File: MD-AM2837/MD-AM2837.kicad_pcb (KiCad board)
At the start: 2 copper layers, 47 x 36 mm, 15 parts, among them J1 XT60_Male_Horizontal, J2 XT60_Female_Horizontal, J3 Conn_01x03_Pin_signal

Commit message: v0.1
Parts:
- added D1: 1N4007, Diode_THT:D_DO-41_SOD81_P10.16mm_Horizontal, F.Cu at (112.5, 87.7)
- added D2: 1N4007, Diode_THT:D_DO-41_SOD81_P10.16mm_Horizontal, F.Cu at (116.0, 87.6)
- added LED4: PWR, LED_SMD:LED_0603_1608Metric_Pad1.05x0.95mm_HandSolder, F.Cu at (90.0, 87.0)
- added Q1: BSS138, Package_TO_SOT_SMD:SOT-23, F.Cu at (106.6, 74.5)
- added Q2: BSS138, Package_TO_SOT_SMD:SOT-23, F.Cu at (106.4, 79.0)
- added R4: R10k, Resistor_SMD:R_0603_1608Metric_Pad0.98x0.95mm_HandSolder, F.Cu at (93.0, 86.1)
- C1: footprint Capacitor_SMD:C_Elec_10x10.2 -> Capacitor_THT:C_Radial_D8.0mm_H11.5mm_P3.50mm
- moved C1 7.40 mm to (125.0, 80.5)
- moved G*** 2.16 mm to (111.0, 82.5)
- moved J2 1.65 mm to (96.4, 91.0)
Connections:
- net Net-(J2-GND) renamed OUT_B
- net Net-(J2-VOUT) renamed OUT_A
- J3 pad 1: Net-(J3-Pin_1) -> IN_A
- J3 pad 2: Net-(J3-Pin_2) -> IN_B
- MD1 pad 1: Net-(J3-Pin_1) -> IN_A
- MD1 pad 2: Net-(J3-Pin_2) -> IN_B
- R1 pad 2: Net-(J3-Pin_1) -> Net-(Q1-D)
- R2 pad 2: Net-(J3-Pin_2) -> Net-(Q2-D)
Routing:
- net Net-(D1-K): track 0.00 -> 41.6 mm
- net Net-(Q1-D): track 0.00 -> 35.5 mm, vias 0 -> 2
- net Net-(J3-Pin_1): track 32.3 -> 0.00 mm
- net IN_A: track 0.00 -> 27.2 mm
- net OUT_B: track 30.2 -> 57.2 mm
- net Net-(J3-Pin_2): track 25.6 -> 0.00 mm
- net Net-(Q2-D): track 0.00 -> 24.0 mm, vias 0 -> 2
- net IN_B: track 0.00 -> 22.8 mm, vias 0 -> 2
- net OUT_A: track 30.5 -> 50.0 mm
- net Net-(LED4-K): track 0.00 -> 4.70 mm
- net VCC: track 97.4 -> 94.7 mm, vias 3 -> 2
- net GND: vias 21 -> 20
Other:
- board text added: "Female"
- board text added: "MD-AM2837 Sep. 11th 2025 Eita TSUGUTA"
- board text added: "Male"
- board text added: "ver. 0.1"
- board text removed: "MD using AM2837 Sep. 30th 2024 Eita TSUGUTA"
- board text removed: "XT60 Female"
- board text removed: "XT60 Male"

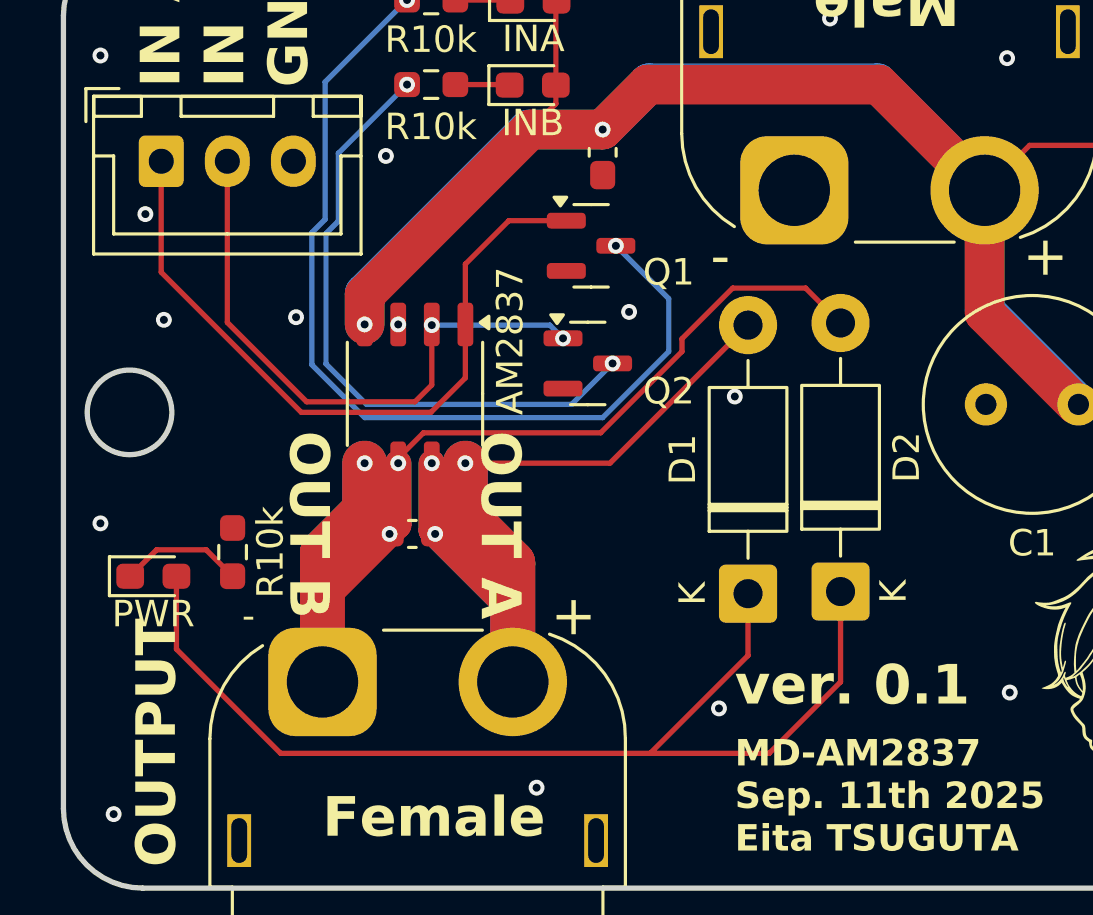
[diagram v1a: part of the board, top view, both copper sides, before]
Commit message: フォトカプラ追加中
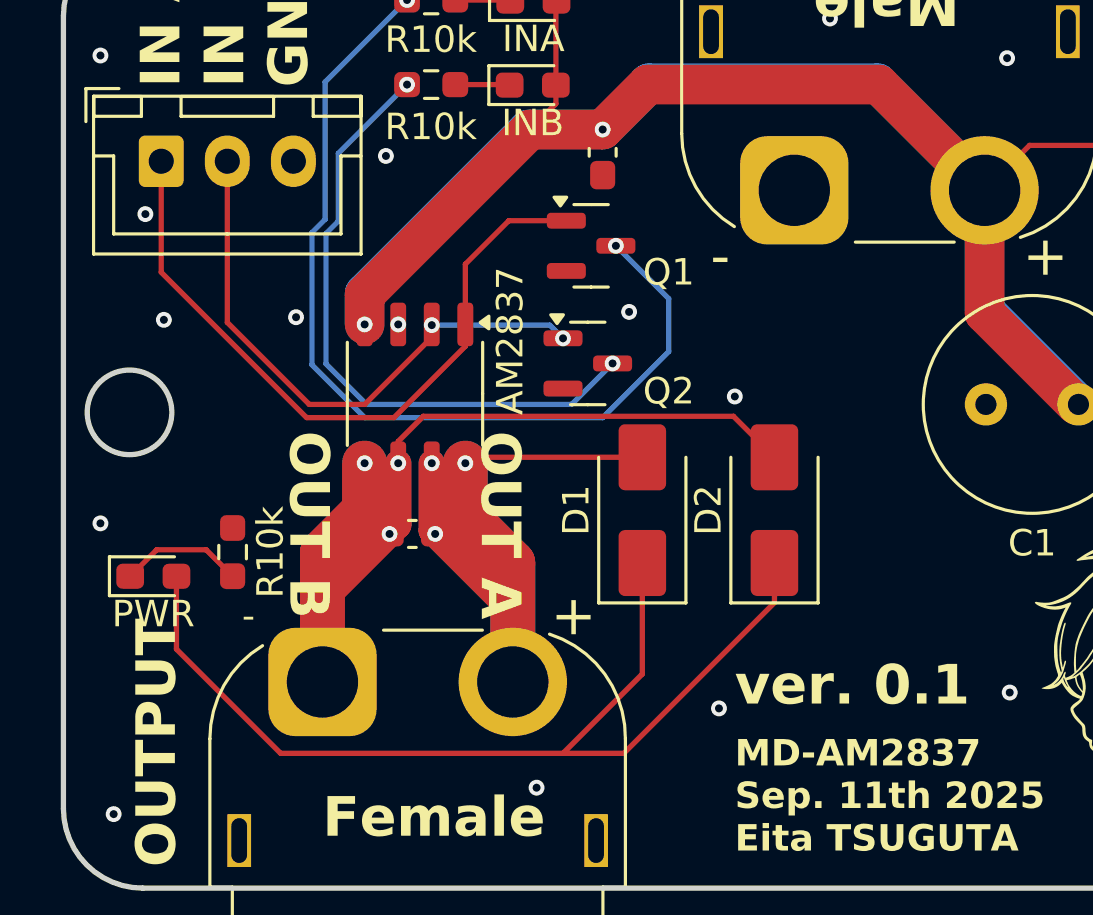
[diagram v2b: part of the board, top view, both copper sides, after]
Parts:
- D1, D2: value 1N4007 -> SS14; footprint Diode_THT:D_DO-41_SOD81_P10.16mm_Horizontal -> Diode_SMD:D_SMA
- moved D1 5.10 mm to (108.5, 84.5)
- moved D2 3.97 mm to (113.5, 84.5)
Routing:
- net OUT_A: track 50.0 -> 43.9 mm
- net OUT_B: track 57.2 -> 52.9 mm
- net Net-(D1-K): track 41.6 -> 39.3 mm
- net IN_B: track 22.8 -> 21.8 mm
- net IN_A: track 27.2 -> 26.7 mm

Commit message: v0.2作成
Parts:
- added C4: 0.1, Capacitor_SMD:C_0603_1608Metric_Pad1.08x0.95mm_HandSolder, F.Cu at (115.9, 93.3)
- added C5: 0.1, Capacitor_SMD:C_0603_1608Metric_Pad1.08x0.95mm_HandSolder, F.Cu at (121.4, 93.3)
- added R10: 1k, Resistor_SMD:R_0603_1608Metric_Pad0.98x0.95mm_HandSolder, F.Cu at (129.6, 72.7)
- added R5: 10k, Resistor_SMD:R_0603_1608Metric_Pad0.98x0.95mm_HandSolder, F.Cu at (125.4, 72.7)
- added R6: 10k, Resistor_SMD:R_0603_1608Metric_Pad0.98x0.95mm_HandSolder, F.Cu at (125.4, 75.8)
- added R7: 1k, Resistor_SMD:R_0603_1608Metric_Pad0.98x0.95mm_HandSolder, F.Cu at (129.6, 75.8)
- added R8: 10, Resistor_SMD:R_0603_1608Metric_Pad0.98x0.95mm_HandSolder, F.Cu at (115.9, 79.7)
- added R9: 10, Resistor_SMD:R_0603_1608Metric_Pad0.98x0.95mm_HandSolder, F.Cu at (121.4, 79.7)
- added U1: TLP2745, Package_SO:SO-6L_10x3.84mm_P1.27mm, F.Cu at (115.8, 86.4)
- added U2: TLP2745, Package_SO:SO-6L_10x3.84mm_P1.27mm, F.Cu at (121.4, 86.4)
- C1: value 220uF -> 220
- C2, C3: value 0.1uF -> 0.1
- R1, R2, R3, R4: value R10k -> 1k
- moved LED3 41.6 mm to (89.5, 66.0), turned to 180 degrees
- moved R3 41.6 mm to (89.5, 69.0)
- moved R2 29.5 mm to (130.0, 69.9), turned to -90 degrees
- moved J3 28.2 mm to (118.0, 66.0)
- moved R1 26.9 mm to (127.0, 69.9), turned to -90 degrees
- moved LED2 25.7 mm to (130.0, 66.4), turned to 90 degrees
- moved LED1 22.6 mm to (127.0, 66.4), turned to 90 degrees
- moved J1 18.0 mm to (96.4, 70.5)
- moved Q2 16.2 mm to (121.7, 73.5), turned to 90 degrees
- moved C1 15.7 mm to (110.2, 75.2), turned to 0 degrees
- moved C2 13.4 mm to (94.4, 75.4), turned to 0 degrees
- moved Q1 11.7 mm to (118.2, 73.5), turned to 90 degrees
- moved LED4 9.01 mm to (89.5, 96.0)
- moved R4 7.75 mm to (89.5, 93.0), turned to 180 degrees
- moved D1 1.90 mm to (106.6, 84.4)
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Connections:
- J3 pad 1: IN_A -> IN_A_1
- J3 pad 2: IN_B -> IN_B_1
- J3 pad 3: GND -> GNDS
- MD1 pad 1: IN_A -> IN_A_2
- MD1 pad 2: IN_B -> IN_B_2
- Q1 pad 1: IN_A -> Net-(Q1-G)
- Q2 pad 1: IN_B -> Net-(Q2-G)
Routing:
- net IN_B_2: track 0.00 -> 70.1 mm
- net IN_A_2: track 0.00 -> 54.0 mm
- net OUT_A: track 43.9 -> 4.93 mm
- net OUT_B: track 52.9 -> 14.7 mm
- net IN_A: track 26.7 -> 0.00 mm
- net Net-(Q1-D): track 35.5 -> 9.51 mm, vias 2 -> 0
- net GNDS: track 0.00 -> 23.6 mm, vias 0 -> 1
- net IN_B: track 21.8 -> 0.00 mm, vias 2 -> 0
- net IN_B_1: track 0.00 -> 17.2 mm, vias 0 -> 2
- net Net-(Q2-D): track 24.0 -> 9.01 mm, vias 2 -> 0
- net IN_A_1: track 0.00 -> 14.9 mm, vias 0 -> 2
- net Net-(Q1-G): track 0.00 -> 12.4 mm
- net Net-(Q2-G): track 0.00 -> 8.89 mm
- net GND: track 0.00 -> 3.54 mm, vias 20 -> 9
- net Vcc_U2: track 0.00 -> 2.29 mm
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- added copper zone on B.Cu, net OUT_A
- added copper zone on F.Cu, net OUT_A
- added copper zone on B.Cu, net OUT_B
- added copper zone on F.Cu, net OUT_B
- added copper zone on B.Cu, net VCC
- added copper zone on F.Cu, net VCC
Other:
- board text added: "MD-AM2837 Sep. 27th 2025 Eita TSUGUTA"
- board text added: "OUT B OUT A"
- board text added: "XH3"
- board text added: "ver. 0.2"
- board text removed: "MD-AM2837 Sep. 11th 2025 Eita TSUGUTA"
- board text removed: "OUT A OUT B"
- board text removed: "ver. 0.1"
